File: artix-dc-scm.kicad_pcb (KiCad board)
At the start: 8 copper layers, 90 x 120.4 mm, 442 parts, among them IC1 TPS54561, J1 RJMG1BD3B8K1ANR, J12 S2B-PH-K-S_LF__SN_, J13 62000311121, J2 1-2199230-6, J3 543630489, J4 M20-7830642, J5 SFF-TA-1002-4C+, J6 0878311420, J7 61300611121, Q1 IRLML6402TRPBF, Q10 2N7002, Q11 2N7002, Q12 2N7002, Q13 2N7002, Q14 2N7002, Q15 2N7002, Q16 2N7002, Q2 IRLML6402TRPBF, Q3 IRLML6402TRPBF, Q4 IRLML6402TRPBF, Q5 IRLML6402TRPBF, Q6 IRLML6402TRPBF, Q7 2N7002, Q8 2N7002, Q9 2N7002, U1 DP83848JSQ_NOPB, U10 TPS62823DLCT, U11 TPS62823DLCT, U12 TPS62823DLCT, U13 TPS62823DLCT, U14 XC7A100T-FGG484, U15 SN74LVC1G08DCKR, U16 SN74LS08DBR, U17 EMMC04G-S100-B08U, U18 MAX3421EEHJ, U19 FT245RQ, U2 W25Q32JVSSIQ_TR, U3 W25Q32JVSSIQ_TR, U4 W25Q32JVSSIQ_TR, U5 W25Q32JVSSIQ_TR, U6 NVT2008DQ,115, U7 AS4C256M16D3, U8 TPS51200DRC, U9 LM3881MME_NOPB, Y1 ABM8G-12.000MHZ-18-D2Y-T, Y2 ABM8G-25.000MHZ-18-D2Y-T

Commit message: Fix in libs
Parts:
- D14, D15: footprint antmicro-footprints:PGB1010603MR -> artix-dc-scm-footprints:PGB1010603MR
- SP1: footprint antmicro-footprints:9774025151 -> artix-dc-scm-footprints:9774025151
- U1: footprint antmicro-footprints:DP83848JSQ-NOPB -> artix-dc-scm-footprints:DP83848JSQ-NOPB
- U18: footprint antmicro-footprints:TQFP-32_5x5mm -> artix-dc-scm-footprints:TQFP-32_5x5mm
- U19: footprint antmicro-footprints:QFN-32-1EP_5x5mm -> artix-dc-scm-footprints:QFN-32-1EP_5x5mm
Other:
- board text removed: "Ethernet"
- board text removed: "M.2 SSD"

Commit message: Update component libraries
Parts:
- FB2: footprint antmicro-footprints:0805-res -> artix-dc-scm-footprints:0805-res
- J1: footprint antmicro-footprints:CONN_RJMG1BD3B8K1ANR -> artix-dc-scm-footprints:CONN_RJMG1BD3B8K1ANR
- TP12, TP13, TP14, TP15, TP2, TP5, TP6: footprint antmicro-footprints:Testpoint_smd_1mm -> artix-dc-scm-footprints:Testpoint_smd_1mm
- U17: footprint antmicro-footprints:MICRON_EMMC_153 -> artix-dc-scm-footprints:MICRON_EMMC_153
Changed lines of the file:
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@@
     )
   )
-  (module antmicro-footprints:Testpoint_smd_1mm (layer F.Cu)
+  (module artix-dc-scm-footprints:Testpoint_smd_1mm (layer F.Cu)
     (at 192.05 104.675)
     (attr virtual)
@@
     )
   )
-  (module antmicro-footprints:CONN_RJMG1BD3B8K1ANR (layer F.Cu)
+  (module artix-dc-scm-footprints:CONN_RJMG1BD3B8K1ANR (layer F.Cu)
     (at 128.425 69.55 180)
     (fp_text reference J1 (at -4.82751 -12.39143) (layer F.SilkS)
@@
     )
   )
-  (module antmicro-footprints:MICRON_EMMC_153 (layer F.Cu)
+  (module artix-dc-scm-footprints:MICRON_EMMC_153 (layer F.Cu)
     (at 129.94 144.445)
     (fp_text reference U17 (at -2.96 -7.25) (layer F.SilkS)
@@
     )
   )
-  (module antmicro-footprints:Testpoint_smd_1mm (layer F.Cu)
+  (module artix-dc-scm-footprints:Testpoint_smd_1mm (layer F.Cu)
     (at 196.064999 100.245799)
     (attr virtual)
@@
       (net 144 PRSNT1_N))
   )
-  (module antmicro-footprints:Testpoint_smd_1mm (layer F.Cu)
+  (module artix-dc-scm-footprints:Testpoint_smd_1mm (layer F.Cu)
     (at 196.064999 102.245799)
     (attr virtual)
@@
       (net 437 "Net-(J2-Pad52)"))
   )
-  (module antmicro-footprints:Testpoint_smd_1mm (layer F.Cu)
+  (module artix-dc-scm-footprints:Testpoint_smd_1mm (layer F.Cu)
     (at 197.8 101.475)
     (attr virtual)
@@
       (net 5 VCC5V0))
   )
-  (module antmicro-footprints:Testpoint_smd_1mm (layer F.Cu)
+  (module artix-dc-scm-footprints:Testpoint_smd_1mm (layer F.Cu)
     (at 174.249999 105.710799)
     (attr virtual)
@@
       (net 283 PROGRAM))
   )
-  (module antmicro-footprints:Testpoint_smd_1mm (layer F.Cu)
+  (module artix-dc-scm-footprints:Testpoint_smd_1mm (layer F.Cu)
     (at 176.889999 103.250799)
     (attr virtual)
@@
       (net 284 INIT))
   )
-  (module antmicro-footprints:Testpoint_smd_1mm (layer F.Cu)
+  (module artix-dc-scm-footprints:Testpoint_smd_1mm (layer F.Cu)
     (at 176.889999 101.250799)
     (attr virtual)
@@
     )
   )
-  (module antmicro-footprints:0805-res (layer F.Cu)
+  (module artix-dc-scm-footprints:0805-res (layer F.Cu)
     (at 120.875 86.675 90)
     (attr smd)

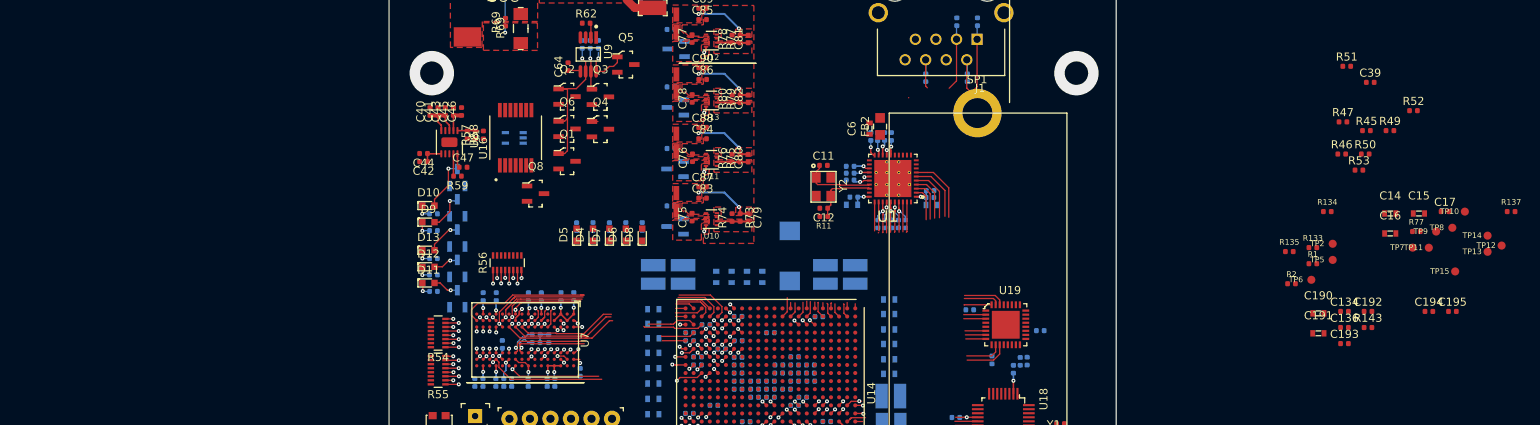
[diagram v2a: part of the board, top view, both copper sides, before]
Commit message: Add simple stackup description
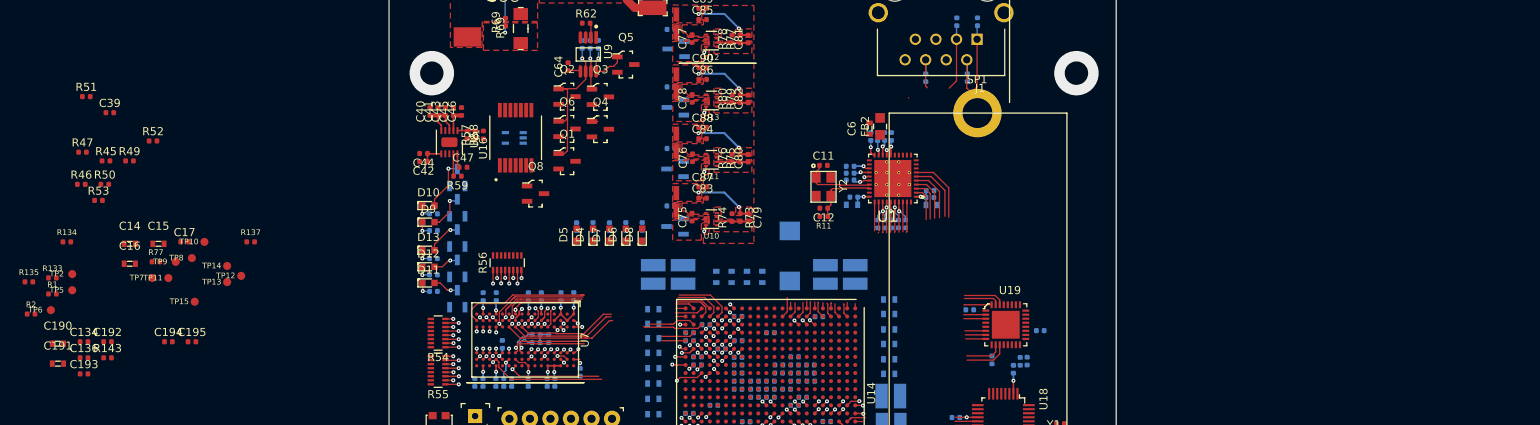
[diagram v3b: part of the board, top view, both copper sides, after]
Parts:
- moved C134 156.0 mm to (22.4, 113.3)
- moved C136 156.0 mm to (22.4, 115.3)
- moved C14 156.0 mm to (28.0, 101.2)
- moved C15 156.0 mm to (31.6, 101.2)
- moved C16 156.0 mm to (28.0, 103.7)
- moved C17 156.0 mm to (34.8, 101.0)
- moved C190 156.0 mm to (19.1, 113.6)
- moved C191 156.0 mm to (19.1, 116.0)
- moved C192 156.0 mm to (25.3, 113.3)
- moved C193 156.0 mm to (22.4, 117.3)
- moved C194 156.0 mm to (32.8, 113.3)
- moved C195 156.0 mm to (35.7, 113.3)
- moved C39 156.0 mm to (25.5, 85.0)
- moved R1 156.0 mm to (18.4, 107.4)
- moved R133 156.0 mm to (18.4, 105.4)
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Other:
- board text added: "1. Copper F.Cu 0.035 -- 2116 0.12 4.5 2. Copper GND1 0.035 -- FR4 0.23 4.6 3. Copper In2 0.035 -- 7630 0.2 4.7 4. Copper VCC1 0.035 -- FR4 0.23 4.6 5. Copper GND2 0.035 -- 7630 0.2 4.5 6. Copper In5 0.035 -- FR4 0.23 4.6 7. Copper VCC2 0.035 -- 2116 0.12 4.6 8. Copper B.Cu 0.035"

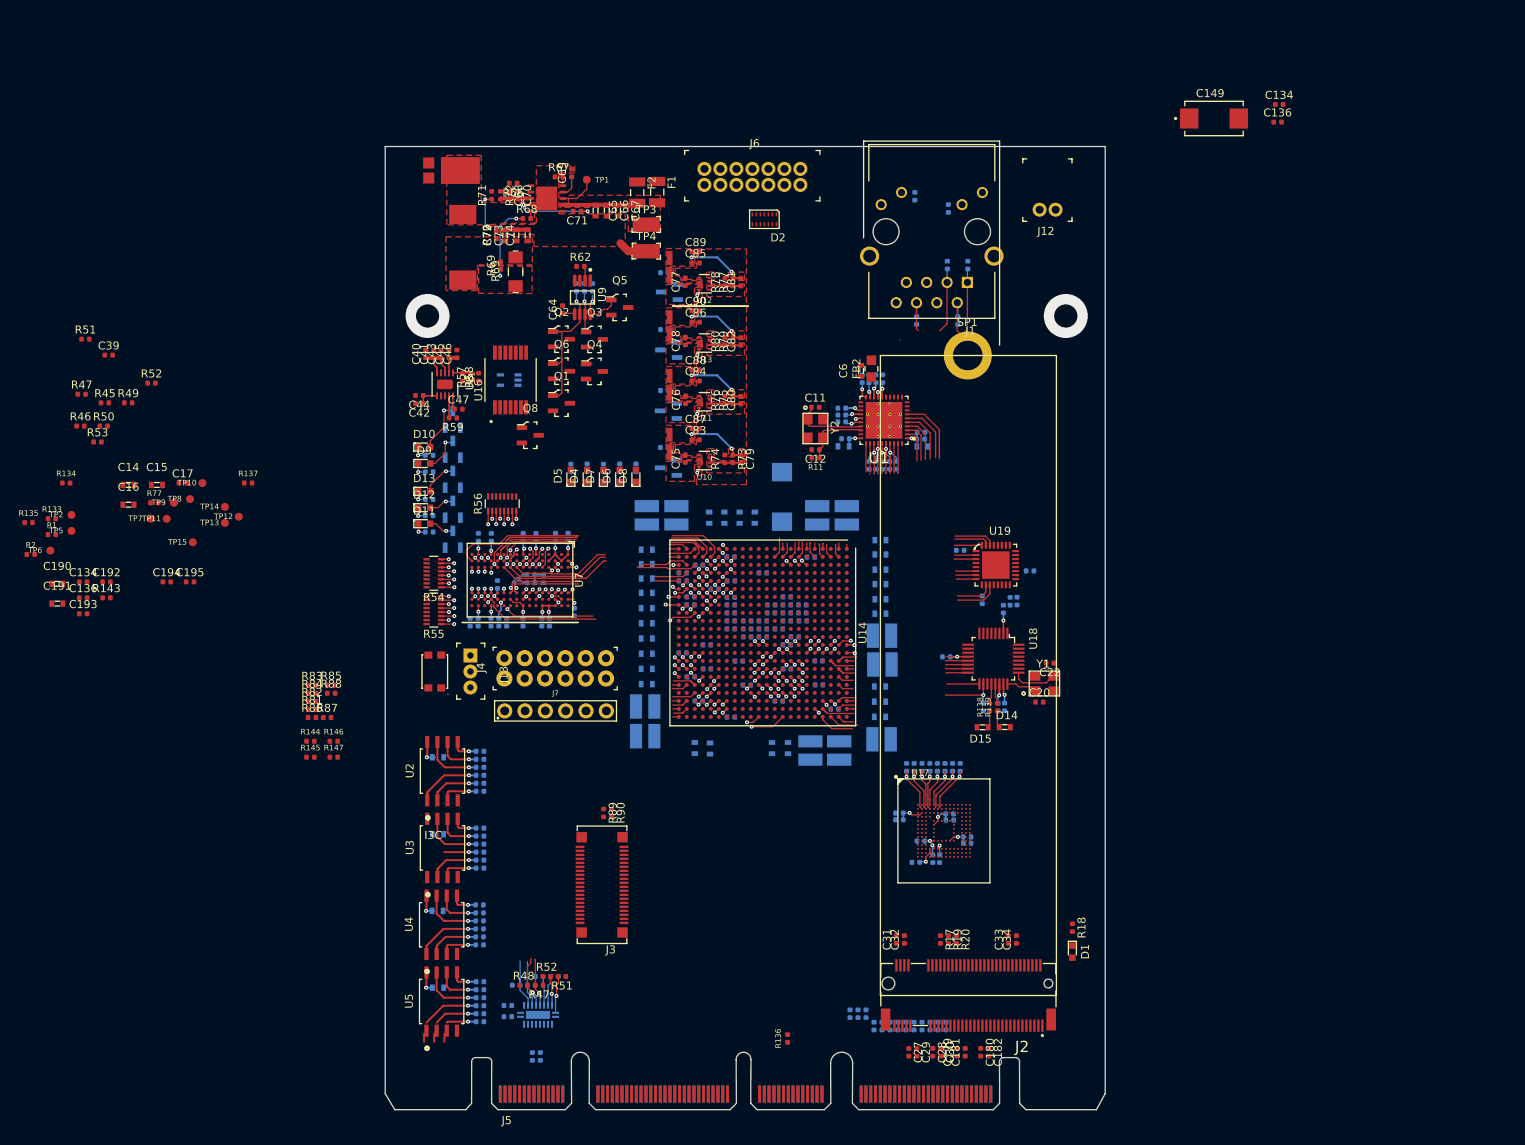
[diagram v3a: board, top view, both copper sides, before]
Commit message: Update naming convention for PCIe
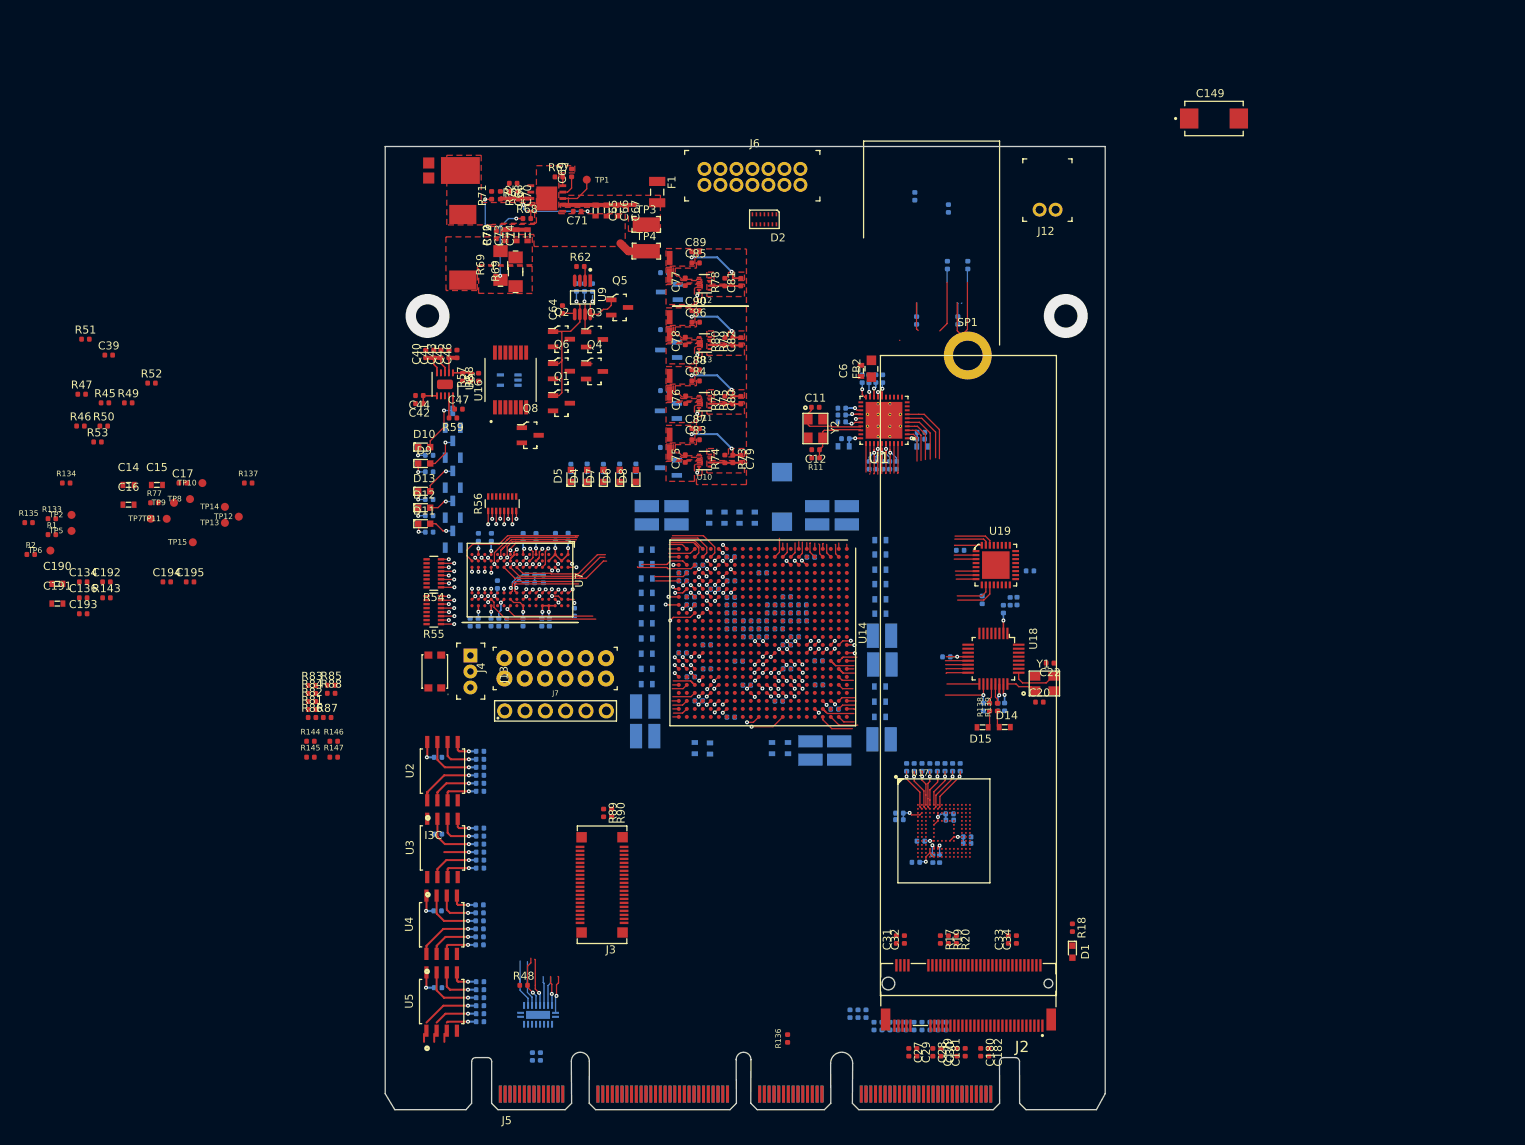
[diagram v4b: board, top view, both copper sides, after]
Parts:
- removed the C134 at (171.8, 53.6)
- removed the C136 at (171.7, 55.9)
- removed the C39 at (75.4, 166.3)
- removed F2: 0466003.NR, artix-dc-scm-footprints:1206-Fuse-Littelfuse-0466-0-0-MFG
- removed J1: RJMG1BD3B8K1ANR, artix-dc-scm-footprints:CONN_RJMG1BD3B8K1ANR
- removed the R45 at (78.4, 163.8)
- removed the R46 at (76.5, 163.7)
- removed the R47 at (79.3, 163.8)
- removed the R49 at (81.3, 162.7)
- removed the R50 at (79.4, 162.7)
- removed the R51 at (82.2, 162.6)
- removed the R52 at (80.3, 162.6)
- removed the R53 at (75.4, 167.7)
- removed the R77 at (103.6, 75.9)
- C35, C36, C37, C38: footprint artix-dc-scm-footprints:0603-cap -> artix-dc-scm-footprints:0402-cap
- R69: footprint artix-dc-scm-footprints:0402-res -> artix-dc-scm-footprints:1206-res
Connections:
- net PCIE_HPM_RXN[0] renamed PCIE_HPM_RX[0]_N
- net PCIE_HPM_RXN[1] renamed PCIE_HPM_RX[1]_N
- net PCIE_HPM_RXN[2] renamed PCIE_HPM_RX[2]_N
- net PCIE_HPM_RXN[3] renamed PCIE_HPM_RX[3]_N
- net PCIE_HPM_RXP[0] renamed PCIE_HPM_RX[0]_P
- net PCIE_HPM_RXP[1] renamed PCIE_HPM_RX[1]_P
- net PCIE_HPM_RXP[2] renamed PCIE_HPM_RX[2]_P
- net PCIE_HPM_RXP[3] renamed PCIE_HPM_RX[3]_P
- net PCIE_HPM_TXN[0] renamed PCIE_HPM_TX[0]_N
- net PCIE_HPM_TXN[1] renamed PCIE_HPM_TX[1]_N
- net PCIE_HPM_TXN[2] renamed PCIE_HPM_TX[2]_N
- net PCIE_HPM_TXN[3] renamed PCIE_HPM_TX[3]_N
- net PCIE_HPM_TXP[0] renamed PCIE_HPM_TX[0]_P
- net PCIE_HPM_TXP[1] renamed PCIE_HPM_TX[1]_P
- net PCIE_HPM_TXP[2] renamed PCIE_HPM_TX[2]_P
- net PCIE_HPM_TXP[3] renamed PCIE_HPM_TX[3]_P
- net RSVD0 renamed PCIE_HPM_CLK_P
- net RSVD1 renamed PCIE_HPM_CLK_N
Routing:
- net Net-(SP1-Pad1): track 0.00 -> 10.5 mm
- net TXP: track 8.22 -> 1.70 mm
- net TXN: track 5.79 -> 1.84 mm

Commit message: Add DRC for PCIe routing
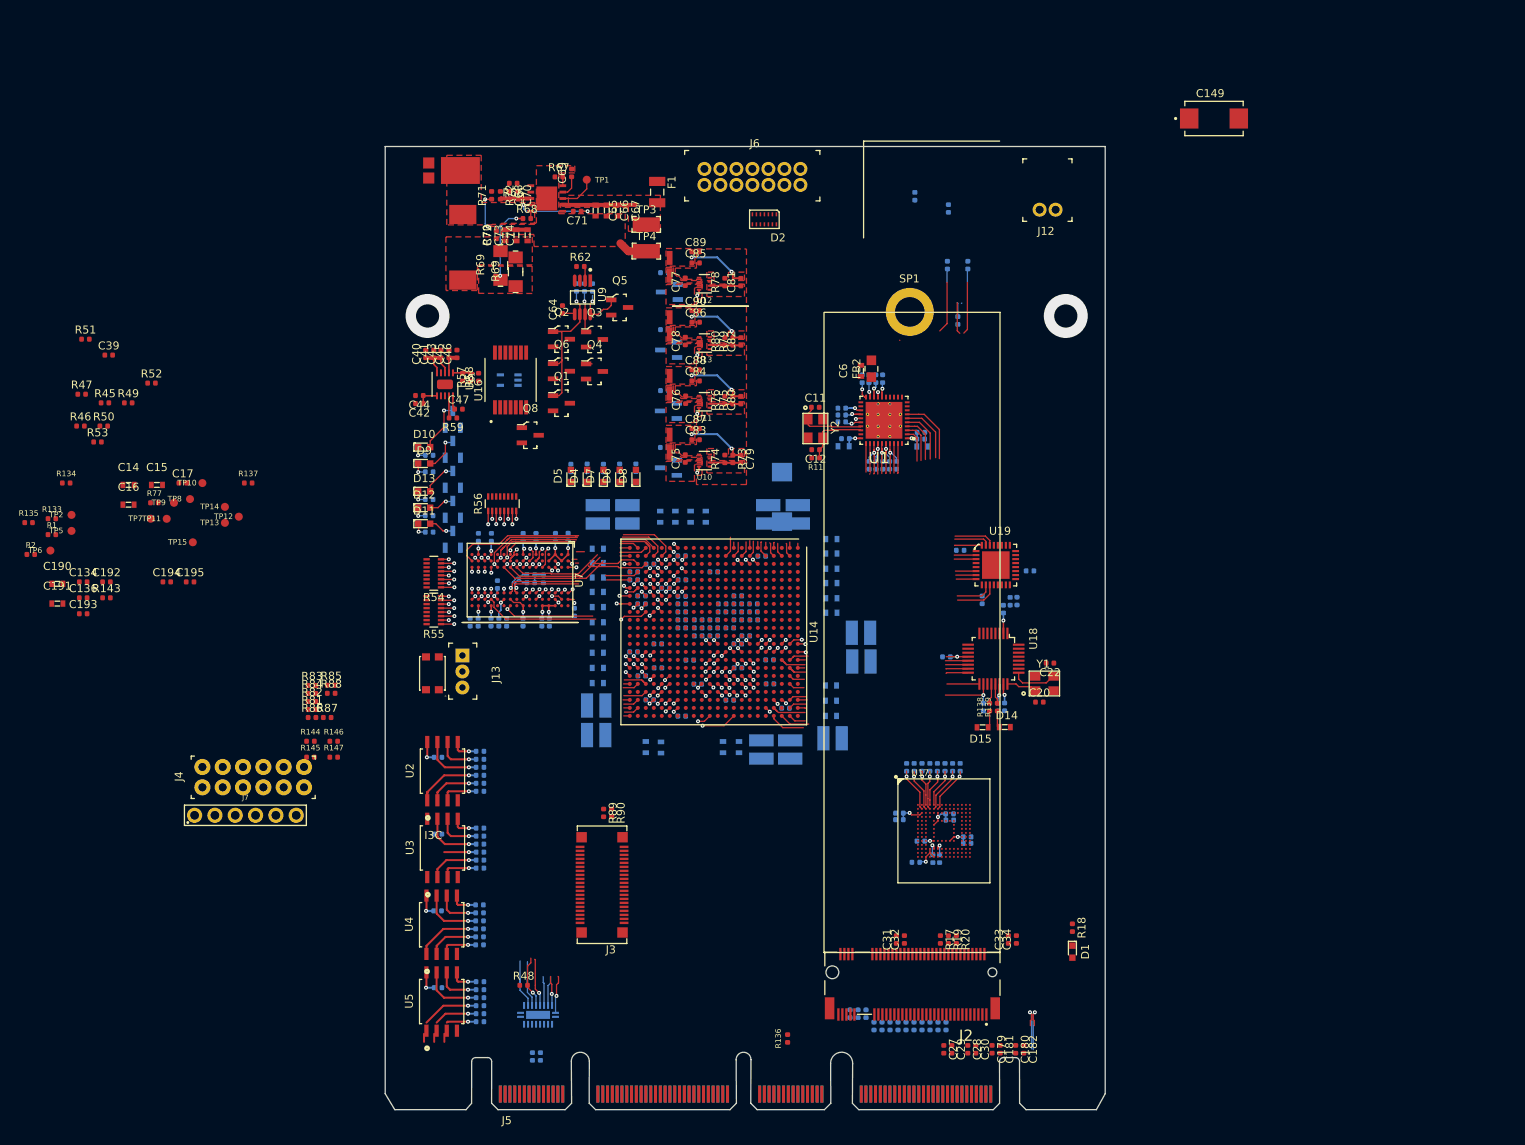
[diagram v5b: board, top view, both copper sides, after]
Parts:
- moved J7 40.9 mm to (42.6, 142.5)
- moved J4 40.1 mm to (37.2, 139.0)
- moved SP1 9.07 mm to (125.6, 79.6)
- moved J2 7.14 mm to (126.0, 162.1)
- moved C100 6.13 mm to (102.3, 134.0)
- moved C101 6.13 mm to (86.7, 111.0)
- moved C102 6.13 mm to (86.7, 112.8)
- moved C103 6.13 mm to (86.7, 126.0)
- moved C104 6.13 mm to (94.6, 134.0)
- moved C105 6.13 mm to (115.9, 109.8)
- moved C106 6.13 mm to (104.3, 134.0)
- moved C107 6.13 mm to (86.7, 109.2)
- moved C108 6.13 mm to (86.7, 114.6)
- moved C109 6.13 mm to (94.2, 124.1)
- moved C110 6.13 mm to (98.2, 123.1)
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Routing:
- net USB1_D6: track 17.0 -> 34.4 mm
- net USB1_D1: track 20.8 -> 3.44 mm
- net USB1_D3: track 15.8 -> 32.3 mm
- net USB1_D7: track 19.9 -> 3.44 mm
- net USB1_D0: track 23.6 -> 33.8 mm
- net I2C[0]_SDA: track 10.9 -> 0.67 mm
- net PCIE_HPM_RX[3]_N: track 0.00 -> 6.57 mm, vias 0 -> 1
- net PCIE_HPM_RX[3]_P: track 0.00 -> 6.47 mm, vias 0 -> 1
- net I2C[8]_SCL: track 3.92 -> 10.3 mm
- net I2C[3]_SDA: track 7.07 -> 0.70 mm
- net DDR3_DQ8: track 14.3 -> 20.4 mm
- net DDR3_DQ11: track 11.4 -> 5.52 mm
- net I2C[12]_SCL: track 2.54 -> 7.97 mm
- net DDR3_DQS0+: track 16.0 -> 10.6 mm
- net DDR3_A11: track 22.4 -> 27.9 mm
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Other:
- net class PCIe added: clearance 0.11, trace_width 0.11, via_dia 0.5, via_drill 0.2
